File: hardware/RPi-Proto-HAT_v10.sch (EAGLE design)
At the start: 36 parts, among them X1 PASSER-07, X2 PASSER-07

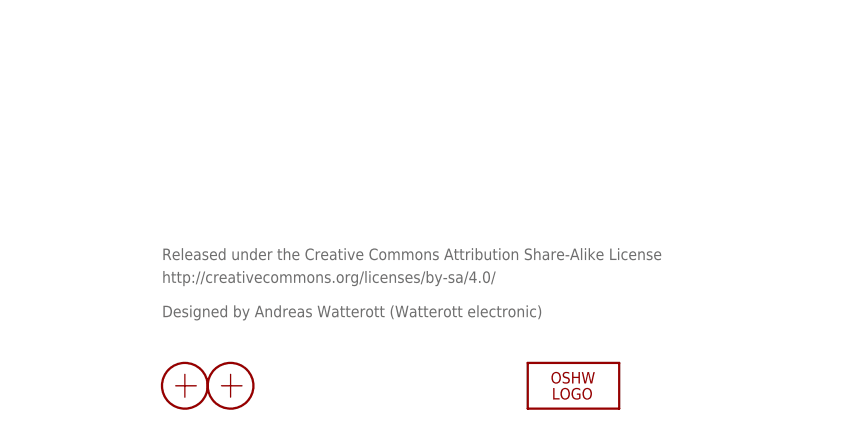
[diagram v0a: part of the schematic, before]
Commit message: updated schematics
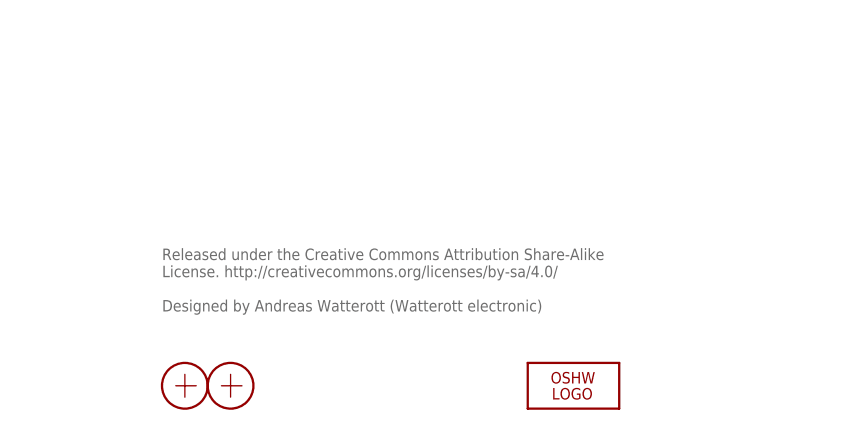
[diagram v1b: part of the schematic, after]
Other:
- note added: "Released under the Creative Commons Attribution Share-Alike License. http://creativecommons.org/licenses/by-sa/4.0/ Designed by Andreas Watterott (Watterott electronic)"
- note removed: "Designed by Andreas Watterott (Watterott electronic)"
- note removed: "Released under the Creative Commons Attribution Share-Alike License"
- note removed: "http://creativecommons.org/licenses/by-sa/4.0/"
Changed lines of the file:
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@@
 <?xml version="1.0" encoding="utf-8"?>
 <!DOCTYPE eagle SYSTEM "eagle.dtd">
-<eagle version="6.6.0">
+<eagle version="7.5.0">
 <drawing>
 <settings>
@@
 <layer number="51" name="tDocu" color="7" fill="1" visible="no" active="no"/>
 <layer number="52" name="bDocu" color="7" fill="1" visible="no" active="no"/>
-<layer number="53" name="tCopper" color="7" fill="11" visible="no" active="no"/>
-<layer number="54" name="bCopper" color="7" fill="1" visible="no" active="no"/>
-<layer number="56" name="wert" color="7" fill="1" visible="no" active="no"/>
-<layer number="57" name="tCAD" color="7" fill="1" visible="no" active="no"/>
 <layer number="91" name="Nets" color="2" fill="1" visible="yes" active="yes"/>
 <layer number="92" name="Busses" color="1" fill="1" visible="yes" active="yes"/>
@@
 <layer number="98" name="Guide" color="6" fill="1" visible="yes" active="yes"/>
 <layer number="99" name="SpiceOrder" color="5" fill="1" visible="yes" active="yes"/>
-<layer number="100" name="Muster" color="7" fill="1" visible="no" active="no"/>
-<layer number="153" name="FabDoc1" color="6" fill="1" visible="no" active="no"/>
-<layer number="154" name="FabDoc2" color="2" fill="1" visible="no" active="no"/>
-<layer number="155" name="FabDoc3" color="7" fill="15" visible="no" active="no"/>
-<layer number="217" name="217bmp" color="18" fill="1" visible="no" active="no"/>
-<layer number="218" name="218bmp" color="19" fill="1" visible="no" active="no"/>
-<layer number="219" name="219bmp" color="20" fill="1" visible="no" active="no"/>
-<layer number="220" name="220bmp" color="21" fill="1" visible="no" active="no"/>
-<layer number="221" name="221bmp" color="22" fill="1" visible="no" active="no"/>
-<layer number="222" name="222bmp" color="23" fill="1" visible="no" active="no"/>
-<layer number="223" name="223bmp" color="24" fill="1" visible="no" active="no"/>
-<layer number="224" name="224bmp" color="25" fill="1" visible="no" active="no"/>
 <layer number="250" name="Descript" color="3" fill="1" visible="yes" active="yes"/>
-<layer number="251" name="SMDround" color="12" fill="11" visible="no" active="no"/>
 </layers>
 <schematic xreflabel="%F%N/%S.%C%R" xrefpart="/%S.%C%R">
@@
 <plain>
 <text x="52.07" y="130.81" size="3.81" layer="250">Raspberry Pi B+</text>
-<text x="162.56" y="21.59" size="1.27" layer="95">Released under the Creative Commons Attribution Share-Alike License</text>
-<text x="162.56" y="19.05" size="1.27" layer="95">http://creativecommons.org/licenses/by-sa/4.0/</text>
-<text x="162.56" y="15.24" size="1.27" layer="95">Designed by Andreas Watterott (Watterott electronic)</text>
+<text x="162.56" y="22.86" size="1.27" layer="95" align="top-left">Released under the Creative Commons Attribution Share-Alike
+License. http://creativecommons.org/licenses/by-sa/4.0/
+Designed by Andreas Watterott (Watterott electronic)</text>
 <text x="152.4" y="130.81" size="3.81" layer="250">ID EEPROM</text>
 <text x="147.32" y="125.73" size="1.27" layer="250" font="vector">OnSemi CAT24C32 or Microchip 24LC32A</text>
@@
 </schematic>
 </drawing>
+<compatibility>
+<note version="6.3" minversion="6.2.2" severity="warning">
+Since Version 6.2.2 text objects can contain more than one line,
+which will not be processed correctly with this version.
+</note>
+</compatibility>
 </eagle>
